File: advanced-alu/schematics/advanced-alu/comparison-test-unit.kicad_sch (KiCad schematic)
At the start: 11 parts, among them U1 74LS04, U18 74LS245, U19 74LS245, U20 74LS682, U21 74LS151, U22 74LS04, U23 74LS08, U4 74LS04, U8 74LS08

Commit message: tweaks and layout improvements
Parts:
- removed U1: 74LS04, symbol 74xx:74LS04
- gave numbers to parts that had none: 1
- renumbered RN2 to RN4, U18 to U19, U19 to U20, U20 to U21, U21 to U22, U22 to U23, U23 to U24, U4 to U3
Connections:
- net at U24.1: now also U12.8, U19.19 (CE)

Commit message: corrected control lines
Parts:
- renumbered U19 to U20, U20 to U21, U21 to U22, U22 to U23, U23 to U24, U24 to U25
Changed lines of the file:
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@@
   (symbol (lib_id "74xx_IEEE:74LS682") (at 143.51 93.98 0) (unit 1)
     (in_bom yes) (on_board yes)
-    (property "Reference" "U21" (id 0) (at 151.765 114.935 0))
+    (property "Reference" "U22" (id 0) (at 151.765 114.935 0))
     (property "Value" "74LS682" (id 1) (at 144.78 93.98 0))
     (property "Footprint" "" (id 2) (at 143.51 93.98 0)
@@
   (symbol (lib_id "74xx:74LS08") (at 208.915 49.53 0) (unit 1)
     (in_bom yes) (on_board yes) (fields_autoplaced)
-    (property "Reference" "U24" (id 0) (at 208.915 42.0202 0))
+    (property "Reference" "U25" (id 0) (at 208.915 42.0202 0))
     (property "Value" "74LS08" (id 1) (at 208.915 44.5571 0))
     (property "Footprint" "" (id 2) (at 208.915 49.53 0)
@@
   (symbol (lib_id "74xx:74LS04") (at 168.275 82.55 0) (unit 1)
     (in_bom yes) (on_board yes) (fields_autoplaced)
-    (property "Reference" "U23" (id 0) (at 168.275 74.7735 0))
+    (property "Reference" "U24" (id 0) (at 168.275 74.7735 0))
     (property "Value" "74LS04" (id 1) (at 168.275 77.5486 0))
     (property "Footprint" "" (id 2) (at 168.275 82.55 0)
@@
   (symbol (lib_id "74xx:74LS151") (at 144.78 151.13 0) (unit 1)
     (in_bom yes) (on_board yes)
-    (property "Reference" "U22" (id 0) (at 153.67 170.815 0)
+    (property "Reference" "U23" (id 0) (at 153.67 170.815 0)
       (effects (font (size 1.27 1.27)) (justify left))
     )
@@
   (symbol (lib_id "74xx:74LS245") (at 82.55 44.45 0) (unit 1)
     (in_bom yes) (on_board yes)
-    (property "Reference" "U19" (id 0) (at 87.63 27.94 0)
+    (property "Reference" "U20" (id 0) (at 87.63 27.94 0)
       (effects (font (size 1.27 1.27)) (justify left))
     )
@@
   (symbol (lib_id "74xx:74LS245") (at 82.55 109.22 0) (unit 1)
     (in_bom yes) (on_board yes)
-    (property "Reference" "U20" (id 0) (at 87.63 92.71 0)
-      (effects (font (size 1.27 1.27)) (justify left))
-    )
+    (property "Reference" "U21" (id 0) (at 87.63 92.71 0)
+      (effects (font (size 1.27 1.27)) (justify left))
+    )

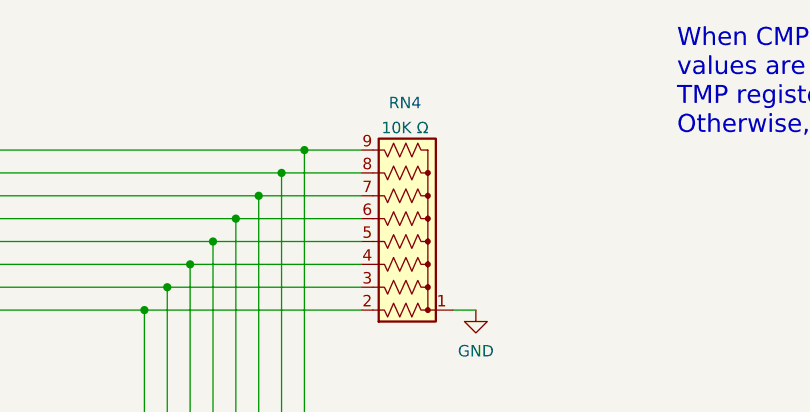
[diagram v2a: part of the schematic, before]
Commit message: fixed bit shifting hardware bug
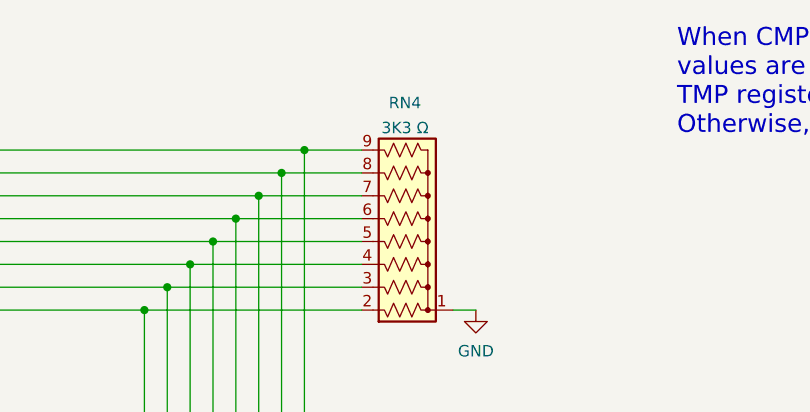
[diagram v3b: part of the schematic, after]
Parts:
- RN4: value 10K Ω -> 3K3 Ω
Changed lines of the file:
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@@
     (in_bom yes) (on_board yes) (fields_autoplaced)
     (property "Reference" "RN4" (id 0) (at 140.716 26.5135 90))
-    (property "Value" "10K Ω" (id 1) (at 140.716 29.2886 90))
+    (property "Value" "3K3 Ω" (id 1) (at 140.716 29.2886 90))
     (property "Footprint" "Resistor_THT:R_Array_SIP9" (id 2) (at 140.97 27.305 90)
       (effects (font (size 1.27 1.27)) hide)
